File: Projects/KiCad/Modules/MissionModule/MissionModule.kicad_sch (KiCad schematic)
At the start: 49 parts, among them J1 Conn_01x08, J2 Micro_SD_Card_Det_Hirose_DM3AT, SW1 SW_DIP_x02, U1 MCP2562-E-P, U2 MCP2515-I/P, U3 NJM7805SDL1, U5 TLP222A, U6 ABX00012, U7 MB85RS2MT, U8 MB85RS2MT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

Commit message: チップ積層セラミックコンデンサをSMD1608に変更
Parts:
- C2, C4, C5, C7: footprint Capacitor_SMD:C_0805_2012Metric_Pad1.18x1.45mm_HandSolder -> Capacitor_SMD:C_0603_1608Metric_Pad1.08x0.95mm_HandSolder
- C3: value 0.33μF -> 10μF; footprint Capacitor_SMD:C_0805_2012Metric_Pad1.18x1.45mm_HandSolder -> Capacitor_SMD:C_0603_1608Metric_Pad1.08x0.95mm_HandSolder
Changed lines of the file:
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@@
       (effects (font (size 1.27 1.27)) (justify left))
     )
-    (property "Footprint" "Capacitor_SMD:C_0805_2012Metric_Pad1.18x1.45mm_HandSolder" (at 249.8852 113.03 0)
+    (property "Footprint" "Capacitor_SMD:C_0603_1608Metric_Pad1.08x0.95mm_HandSolder" (at 249.8852 113.03 0)
       (effects (font (size 1.27 1.27)) hide)
     )
@@
       (effects (font (size 1.27 1.27)) (justify left))
     )
-    (property "Footprint" "Capacitor_SMD:C_0805_2012Metric_Pad1.18x1.45mm_HandSolder" (at 84.7852 31.75 0)
+    (property "Footprint" "Capacitor_SMD:C_0603_1608Metric_Pad1.08x0.95mm_HandSolder" (at 84.7852 31.75 0)
       (effects (font (size 1.27 1.27)) hide)
     )
@@
       (effects (font (size 1.27 1.27)) (justify left))
     )
-    (property "Value" "0.33μF" (at 227.33 111.125 0)
-      (effects (font (size 1.27 1.27)) (justify left))
-    )
-    (property "Footprint" "Capacitor_SMD:C_0805_2012Metric_Pad1.18x1.45mm_HandSolder" (at 224.4852 113.03 0)
+    (property "Value" "10μF" (at 227.33 111.125 0)
+      (effects (font (size 1.27 1.27)) (justify left))
+    )
+    (property "Footprint" "Capacitor_SMD:C_0603_1608Metric_Pad1.08x0.95mm_HandSolder" (at 224.4852 113.03 0)
       (effects (font (size 1.27 1.27)) hide)
     )
@@
       (effects (font (size 1.27 1.27)) (justify left))
     )
-    (property "Footprint" "Capacitor_SMD:C_0805_2012Metric_Pad1.18x1.45mm_HandSolder" (at 127.9652 27.94 0)
+    (property "Footprint" "Capacitor_SMD:C_0603_1608Metric_Pad1.08x0.95mm_HandSolder" (at 127.9652 27.94 0)
       (effects (font (size 1.27 1.27)) hide)
     )
@@
       (effects (font (size 1.27 1.27)) (justify left))
     )
-    (property "Footprint" "Capacitor_SMD:C_0805_2012Metric_Pad1.18x1.45mm_HandSolder" (at 75.8952 31.75 0)
-      (effects (font (size 1.27 1.27)) hide)
-    )
+    (property "Footprint" "Capacitor_SMD:C_0603_1608Metric_Pad1.08x0.95mm_HandSolder" (at 75.8952 31.75 0)
+      (effects (font (size 1.27 1.27)) hide)
+    )

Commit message: 抵抗の在庫に合わせてサイズを変更
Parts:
- R3, R4, R5, R6, R7: footprint Resistor_SMD:R_0603_1608Metric_Pad0.98x0.95mm_HandSolder -> Resistor_SMD:R_0805_2012Metric_Pad1.20x1.40mm_HandSolder
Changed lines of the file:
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@@
       (effects (font (size 1.27 1.27)) (justify left))
     )
-    (property "Footprint" "Resistor_SMD:R_0603_1608Metric_Pad0.98x0.95mm_HandSolder" (at 270.002 46.99 90)
+    (property "Footprint" "Resistor_SMD:R_0805_2012Metric_Pad1.20x1.40mm_HandSolder" (at 270.002 46.99 90)
       (effects (font (size 1.27 1.27)) hide)
     )
@@
       (effects (font (size 1.27 1.27)))
     )
-    (property "Footprint" "Resistor_SMD:R_0603_1608Metric_Pad0.98x0.95mm_HandSolder" (at 133.35 67.818 90)
+    (property "Footprint" "Resistor_SMD:R_0805_2012Metric_Pad1.20x1.40mm_HandSolder" (at 133.35 67.818 90)
       (effects (font (size 1.27 1.27)) hide)
     )
@@
       (effects (font (size 1.27 1.27)) (justify left))
     )
-    (property "Footprint" "Resistor_SMD:R_0603_1608Metric_Pad0.98x0.95mm_HandSolder" (at 280.162 46.99 90)
+    (property "Footprint" "Resistor_SMD:R_0805_2012Metric_Pad1.20x1.40mm_HandSolder" (at 280.162 46.99 90)
       (effects (font (size 1.27 1.27)) hide)
     )
@@
       (effects (font (size 1.27 1.27)) (justify left))
     )
-    (property "Footprint" "Resistor_SMD:R_0603_1608Metric_Pad0.98x0.95mm_HandSolder" (at 230.632 46.99 90)
+    (property "Footprint" "Resistor_SMD:R_0805_2012Metric_Pad1.20x1.40mm_HandSolder" (at 230.632 46.99 90)
       (effects (font (size 1.27 1.27)) hide)
     )
@@
       (effects (font (size 1.27 1.27)) (justify left))
     )
-    (property "Footprint" "Resistor_SMD:R_0603_1608Metric_Pad0.98x0.95mm_HandSolder" (at 220.472 46.99 90)
-      (effects (font (size 1.27 1.27)) hide)
-    )
+    (property "Footprint" "Resistor_SMD:R_0805_2012Metric_Pad1.20x1.40mm_HandSolder" (at 220.472 46.99 90)
+      (effects (font (size 1.27 1.27)) hide)
+    )

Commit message: コネクタのピン配置を変更
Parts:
- J1: footprint Connector_Hirose:Hirose_DF11-8DP-2DSA_2x04_P2.00mm_Vertical -> Hirose_Connector:Hirose_DF11B-8DP-2DS
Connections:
- net CAN_L: now also J1.5 (Pin_5), J1.6 (Pin_6); no longer J1.3 (Pin_3), J1.4 (Pin_4)
- net GND: now also J1.3 (Pin_3), J1.4 (Pin_4); no longer J1.5 (Pin_5), J1.6 (Pin_6)
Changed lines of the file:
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@@
     (stroke (width 0) (type default))
+  )
+  (label "CAN_H" (at 35.56 25.4 180) (fields_autoplaced)
+    (effects (font (size 1.27 1.27)) (justify right bottom))
+  )
+  (label "CAN_H" (at 35.56 53.34 180) (fields_autoplaced)
+    (effects (font (size 1.27 1.27)) (justify right bottom))
+  )
+  (label "CAN_L" (at 35.56 30.48 180) (fields_autoplaced)
+    (effects (font (size 1.27 1.27)) (justify right bottom))
+  )
+  (label "CAN_L" (at 35.56 55.88 180) (fields_autoplaced)
+    (effects (font (size 1.27 1.27)) (justify right bottom))
   )
   (label "+12V" (at 35.56 40.64 180) (fields_autoplaced)
     (effects (font (size 1.27 1.27)) (justify right bottom))
   )
-  (label "CAN_H" (at 35.56 53.34 180) (fields_autoplaced)
-    (effects (font (size 1.27 1.27)) (justify right bottom))
-  )
-  (label "CAN_H" (at 35.56 25.4 180) (fields_autoplaced)
-    (effects (font (size 1.27 1.27)) (justify right bottom))
-  )
-  (label "CAN_L" (at 35.56 55.88 180) (fields_autoplaced)
-    (effects (font (size 1.27 1.27)) (justify right bottom))
-  )
   (label "GND" (at 40.64 55.88 0) (fields_autoplaced)
     (effects (font (size 1.27 1.27)) (justify left bottom))
   )
+  (label "GND" (at 35.56 35.56 180) (fields_autoplaced)
+    (effects (font (size 1.27 1.27)) (justify right bottom))
+  )
   (label "+12V" (at 40.64 53.34 0) (fields_autoplaced)
     (effects (font (size 1.27 1.27)) (justify left bottom))
-  )
-  (label "CAN_L" (at 35.56 35.56 180) (fields_autoplaced)
-    (effects (font (size 1.27 1.27)) (justify right bottom))
-  )
-  (label "GND" (at 35.56 30.48 180) (fields_autoplaced)
-    (effects (font (size 1.27 1.27)) (justify right bottom))
   )
   (global_label "MEMORY_POWER" (shape input) (at 132.08 166.37 0) (fields_autoplaced)
@@
       (effects (font (size 1.27 1.27)))
     )
-    (property "Footprint" "Connector_Hirose:Hirose_DF11-8DP-2DSA_2x04_P2.00mm_Vertical" (at 19.05 34.29 0)
-      (effects (font (size 1.27 1.27)) hide)
-    )
+    (property "Footprint" "Hirose_Connector:Hirose_DF11B-8DP-2DS" (at 19.05 34.29 0)
+      (effects (font (size 1.27 1.27)) hide)
+    )

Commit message: クリスタルをSMDに変更
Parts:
- Y1: footprint Crystal:Crystal_HC49-U_Vertical -> Crystal:Crystal_SMD_HC49-SD
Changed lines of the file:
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@@
       (effects (font (size 1.27 1.27)) (justify right))
     )
-    (property "Footprint" "Crystal:Crystal_HC49-U_Vertical" (at 153.67 88.9 0)
+    (property "Footprint" "Crystal:Crystal_SMD_HC49-SD" (at 153.67 88.9 0)
       (effects (font (size 1.27 1.27)) hide)
     )

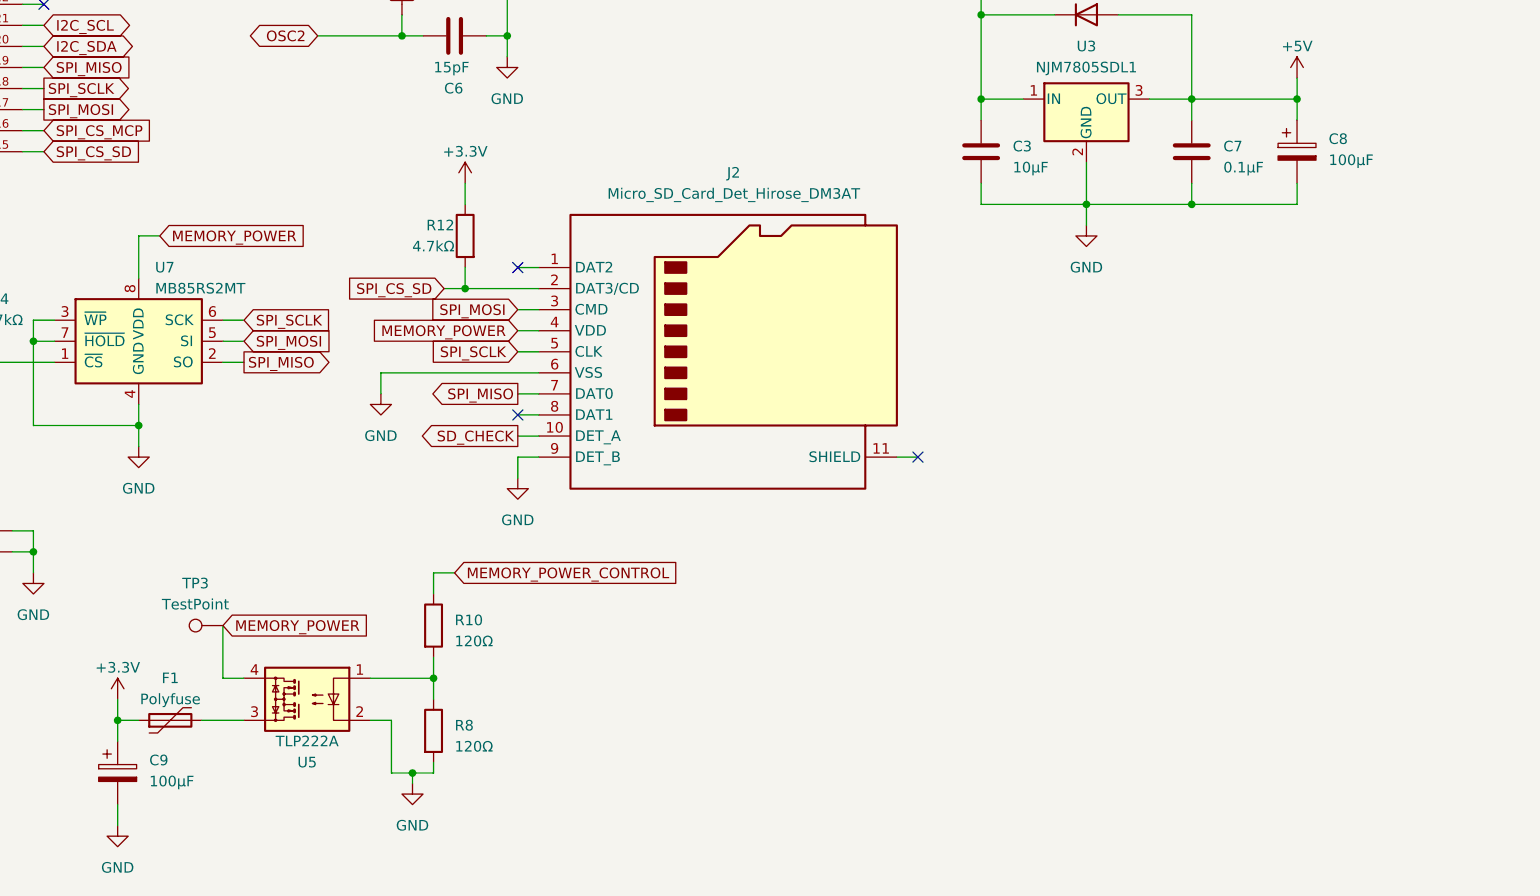
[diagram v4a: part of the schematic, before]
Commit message: バッファコンデンサを表面実装に変更
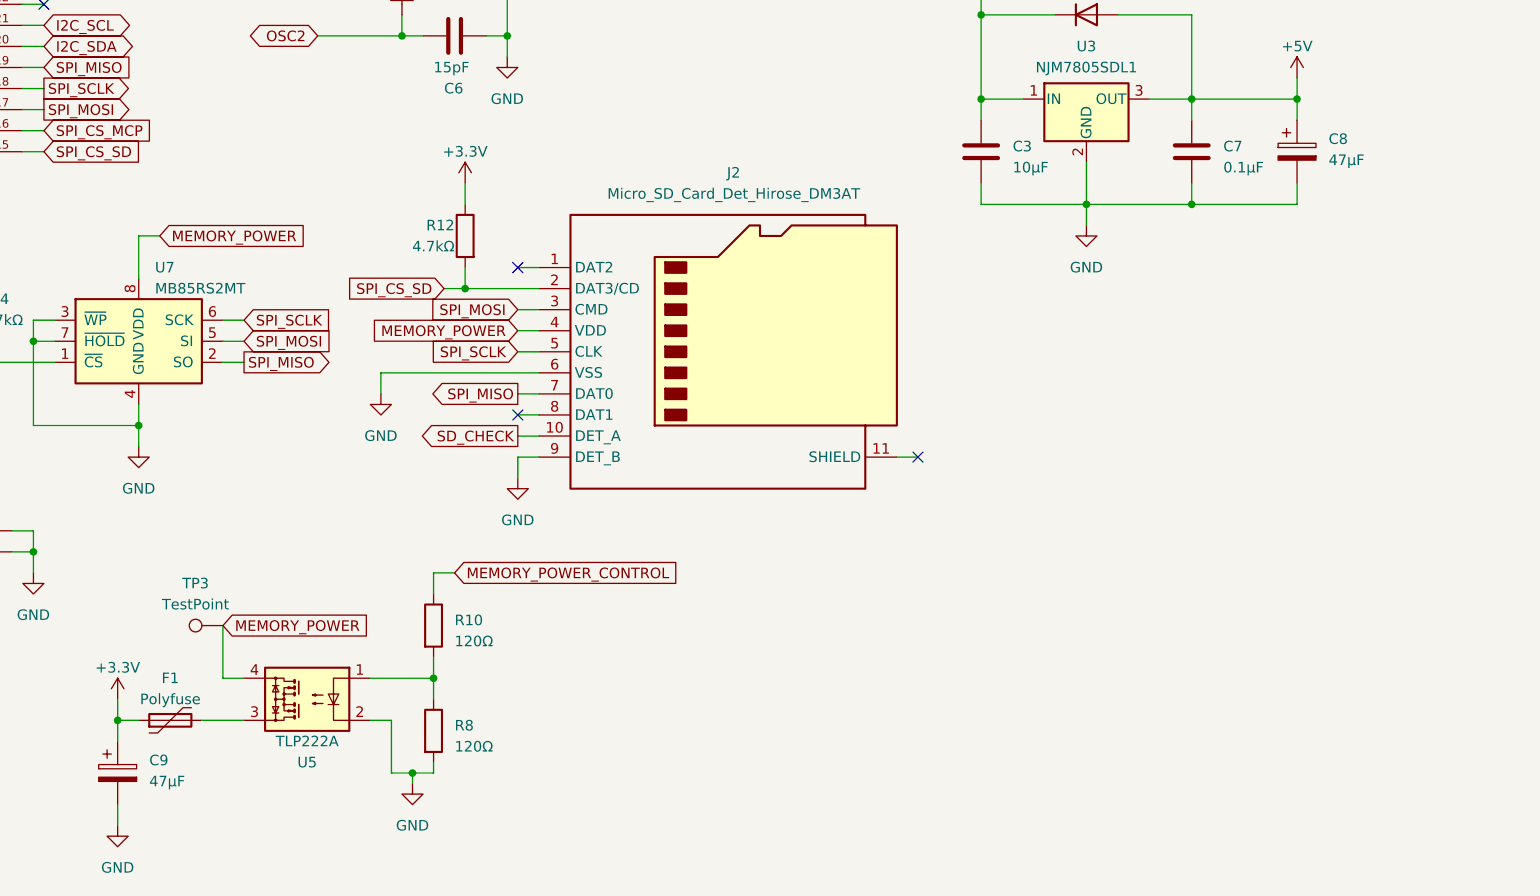
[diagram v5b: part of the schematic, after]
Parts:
- C8, C9: value 100μF -> 47μF; footprint Capacitor_SMD:CP_Elec_6.3x7.7 -> Capacitor_SMD:CP_Elec_6.3x5.9
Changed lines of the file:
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@@
       (effects (font (size 1.27 1.27)) (justify left))
     )
-    (property "Value" "100μF" (at 265.43 110.236 0)
+    (property "Value" "47μF" (at 265.43 110.236 0)
       (effects (font (size 1.27 1.27)) (justify left))
     )
-    (property "Footprint" "Capacitor_SMD:CP_Elec_6.3x7.7" (at 262.5852 113.03 0)
+    (property "Footprint" "Capacitor_SMD:CP_Elec_6.3x5.9" (at 262.5852 113.03 0)
       (effects (font (size 1.27 1.27)) hide)
     )
@@
       (effects (font (size 1.27 1.27)) (justify left))
     )
-    (property "Value" "100μF" (at 123.19 185.166 0)
+    (property "Value" "47μF" (at 123.19 185.166 0)
       (effects (font (size 1.27 1.27)) (justify left))
     )
-    (property "Footprint" "Capacitor_SMD:CP_Elec_6.3x7.7" (at 120.3452 187.96 0)
+    (property "Footprint" "Capacitor_SMD:CP_Elec_6.3x5.9" (at 120.3452 187.96 0)
       (effects (font (size 1.27 1.27)) hide)
     )

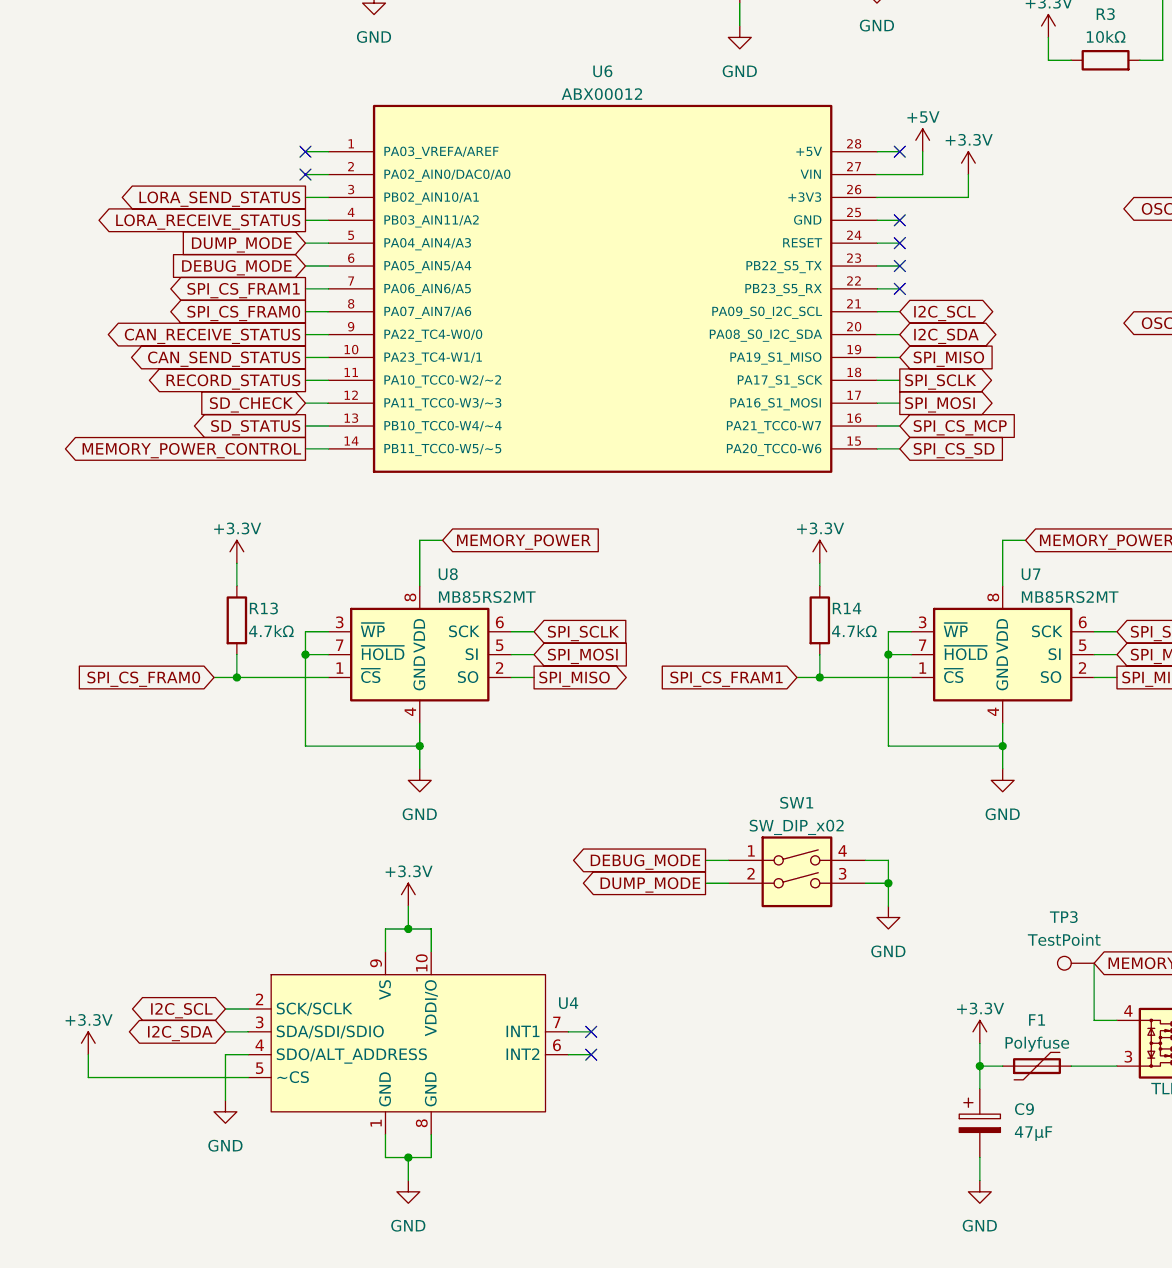
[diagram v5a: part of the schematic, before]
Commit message: ADXLをSPI接続に変更
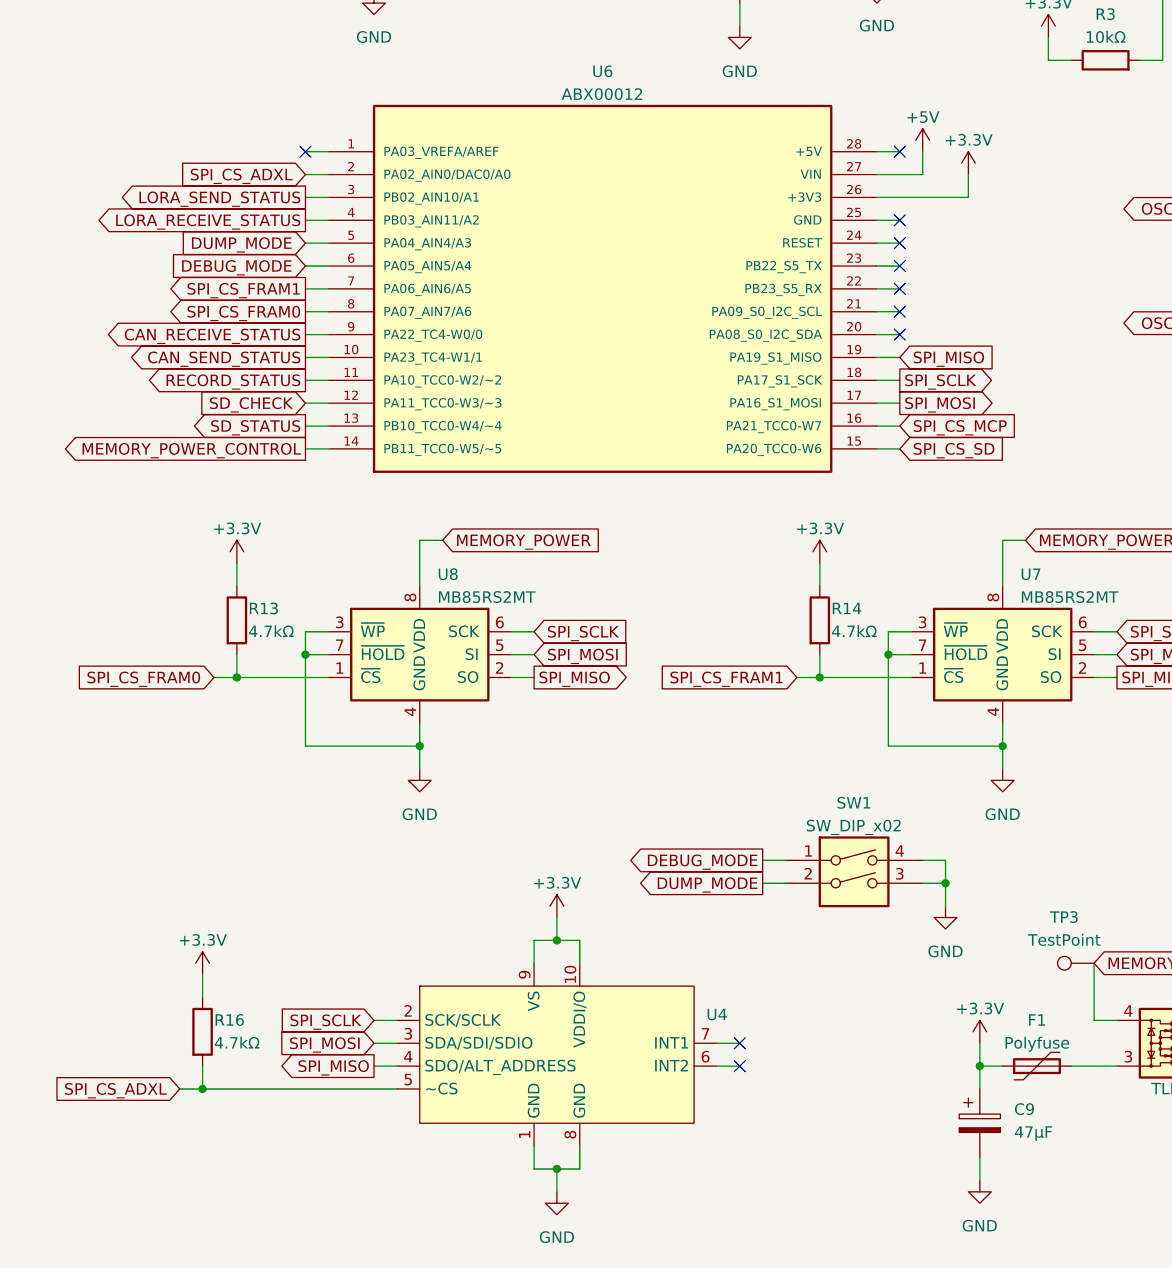
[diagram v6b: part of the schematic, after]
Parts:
- added R16: 4.7kΩ, Resistor_SMD:R_0603_1608Metric_Pad0.98x0.95mm_HandSolder, symbol Device:R
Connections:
- net +3.3V: now also R16.1; no longer U4.5 (~CS)
- net GND: no longer U4.4 (SDO/ALT_ADDRESS)
- net SPI_MISO: now also U4.4 (SDO/ALT_ADDRESS)
- net SPI_MOSI: now also U4.3 (SDA/SDI/SDIO)
- net SPI_SCLK: now also U4.2 (SCK/SCLK)
- net SPI_CS_ADXL: now reaches U6.2 (PA02_AIN0/DAC0/A0)
- net SPI_CS_ADXL: now also U4.5 (~CS), R16.2
- net I2C_SCL: no longer names the net of U6.21 (PA09_S0_I2C_SCL)
- net I2C_SCL: no longer U4.2 (SCK/SCLK)
- net I2C_SDA: no longer names the net of U6.20 (PA08_S0_I2C_SDA)
- net I2C_SDA: no longer U4.3 (SDA/SDI/SDIO)
- no-connect marks 19 -> 20
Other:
- moved on the sheet: SW1, U4
